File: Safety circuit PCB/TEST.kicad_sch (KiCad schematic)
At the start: 35 parts, among them J1 Conn_01x02_Socket, J2 Conn_01x02_Socket, J3 Conn_01x02_Socket, J4 Conn_01x02_Socket, J5 Conn_01x02_Socket, J6 Conn_01x01_Socket, J7 Conn_01x01_Socket, Q10 NMOS, Q11 NMOS, Q12 NMOS, Q6 NMOS, Q7 NMOS, Q8 NMOS, Q9 NMOS

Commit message: Safety Circuit PCB First Prototype
First prototype board and schematic for safety circuit. Falstad simulation for safety circuit demonstrating how it works is https://tinyurl.com/275r7dj9
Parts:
- removed J1, J2, J3, J4, J5: Conn_01x02_Socket, symbol Connector:Conn_01x02_Socket
- removed J6, J7: Conn_01x01_Socket, symbol Connector:Conn_01x01_Socket
- removed Q10, Q11, Q12, Q6, Q7, Q8, Q9: NMOS, symbol Simulation_SPICE:NMOS
- added J1, J2: 430450801, SC:CONN_SD-43045-001_08_MOL, symbol SC:430450801
- added Q1, Q2, Q3, Q4, Q5, Q6, Q7: 2N7002K, Package_TO_SOT_SMD:SOT-23, symbol Transistor_FET:2N7002K
- D10, D11, D12, D6, D7, D8, D9: footprint (none) -> SC:HL-PSC-1608U52GC-G4; JCL Datasheet (none) -> https://jlcpcb.com/api/file/downloadByFileSystemAccessId/85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; JCL Link (none) -> https://jlcpcb.com/partdetail/23857065-PSC_1608U50GCG4/C223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; JCL# (none) -> C22371297; MFR Part # (none) -> PSC-1608U50GC-G4; Manufacturer (none) -> HONGLITRONIC (Hongli Zhihui (HONGLITRONIC))
- R12, R13, R14, R15, R16, R17, R18, R19, R20, R21, R22, R23, R24, R25: value R_US -> 1k; footprint (none) -> SC:CRCW0805; Digikey (none) -> https://www.digikey.com/en/products/detail/vishay-dale/CRCW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; JCL Datasheet (none) -> https://jlcpcb.com/api/file/downloadByFileSystemAccessId/85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; JCL Link (none) -> https://jlcpcb.com/partdetail/VishayIntertech-CRCW08051K00F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; JCL# (none) -> C844939; MFR Part # (none) -> CRCW08051K00FKEA; Manufacturer (none) -> Vishay
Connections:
- net +12V: now also J2.8
- net BOTS: now also J2.2, J2.3, Q6.1 (G); no longer R12.1
- net COCKPIT_BUTTON: now also J1.8, J2.1, Q5.1 (G)
- net GND: now also J2.5, J2.6, J2.7, Q1.2 (S), Q2.2 (S), Q3.2 (S), Q4.2 (S), Q5.2 (S), Q6.2 (S), Q7.2 (S)
- net INERTIA_SWITCH: now also J1.6, J1.7, Q4.1 (G)
- net INPUT: now also J1.1, Q1.1 (G)
- net LEFT_BUTTON: now also J1.2, J1.3, Q2.1 (G)
- net RIGHT_BUTTON: now also J1.4, J1.5, Q3.1 (G)
- net at R19.2: now also Q6.3 (D)
- net at R25.2: now also Q1.3 (D)
- net at R20.2: now also Q5.3 (D)
- net at R21.2: now also Q4.3 (D)
- net at R22.2: now also Q3.3 (D)
- net at R18.2: now also Q7.3 (D)
- net at R23.2: now also Q2.3 (D)
- new net OUTPUT: J2.4, Q7.1 (G), R12.1

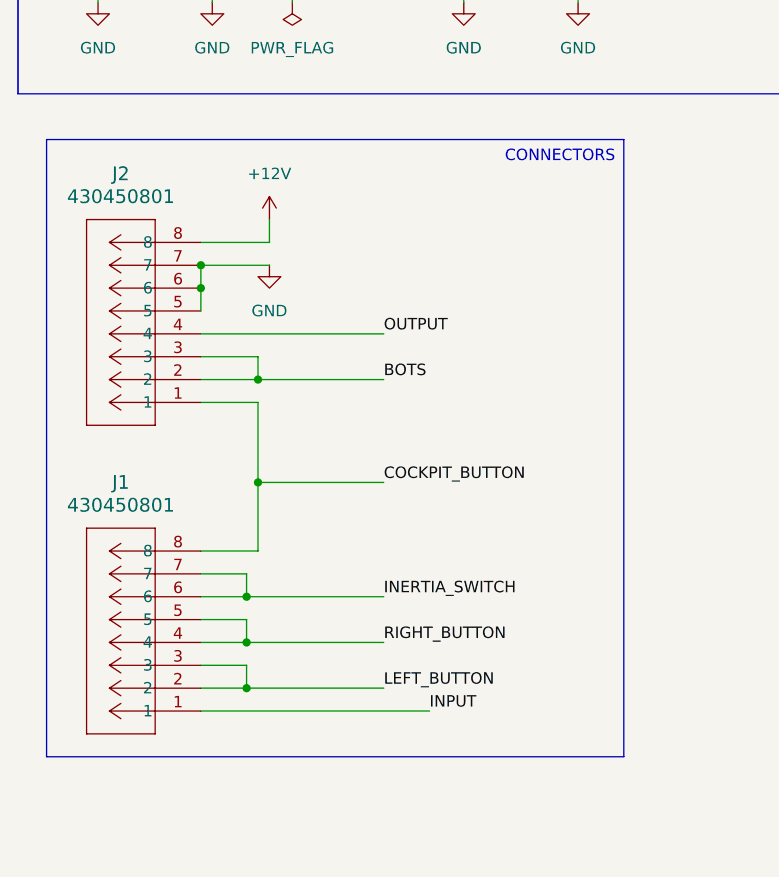
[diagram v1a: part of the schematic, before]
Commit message: Flip connectors, make more sane pin assignments for connections, get nicer tracks, and make dimensions reasonable
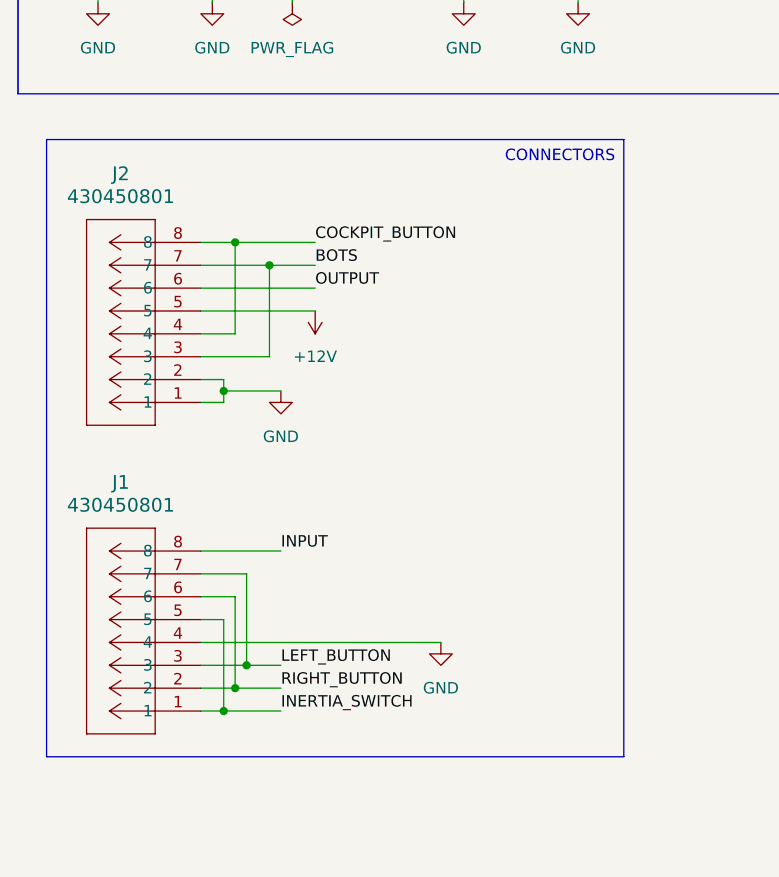
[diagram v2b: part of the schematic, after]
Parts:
- J1, J2: footprint SC:CONN_SD-43045-001_08_MOL -> CONN_SD-43045-001_08_MOL
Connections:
- net +12V: now also J2.5; no longer J2.8
- net BOTS: now also J2.7; no longer J2.2
- net COCKPIT_BUTTON: now also J2.4, J2.8; no longer J1.8, J2.1
- net GND: now also J1.4, J2.1, J2.2; no longer J2.5, J2.6, J2.7
- net INERTIA_SWITCH: now also J1.1, J1.5; no longer J1.6, J1.7
- net INPUT: now also J1.8; no longer J1.1
- net LEFT_BUTTON: now also J1.7; no longer J1.2
- net OUTPUT: now also J2.6; no longer J2.4
- net RIGHT_BUTTON: now also J1.2, J1.6; no longer J1.4, J1.5

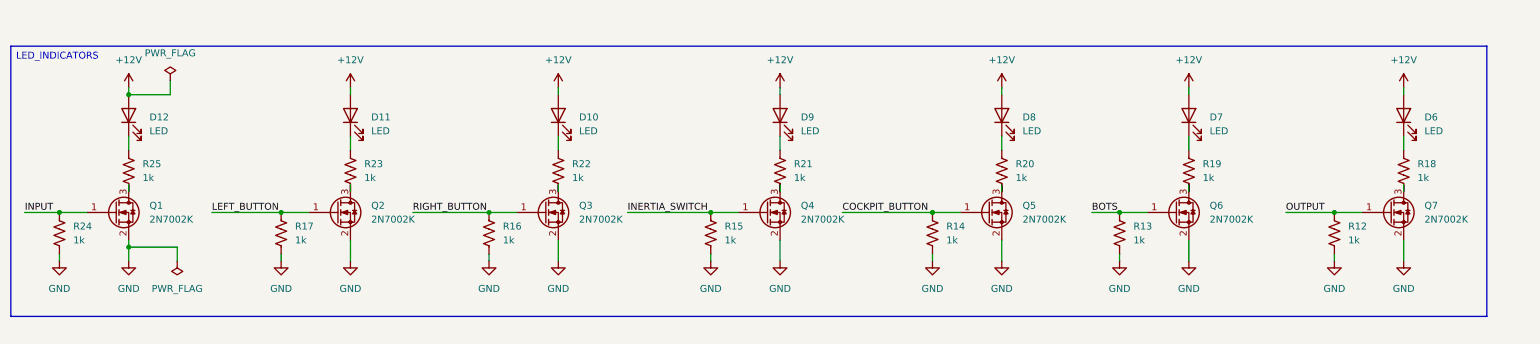
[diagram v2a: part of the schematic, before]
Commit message: Add mounting holes, round corners, add silkscreen logo and Charlie Brown
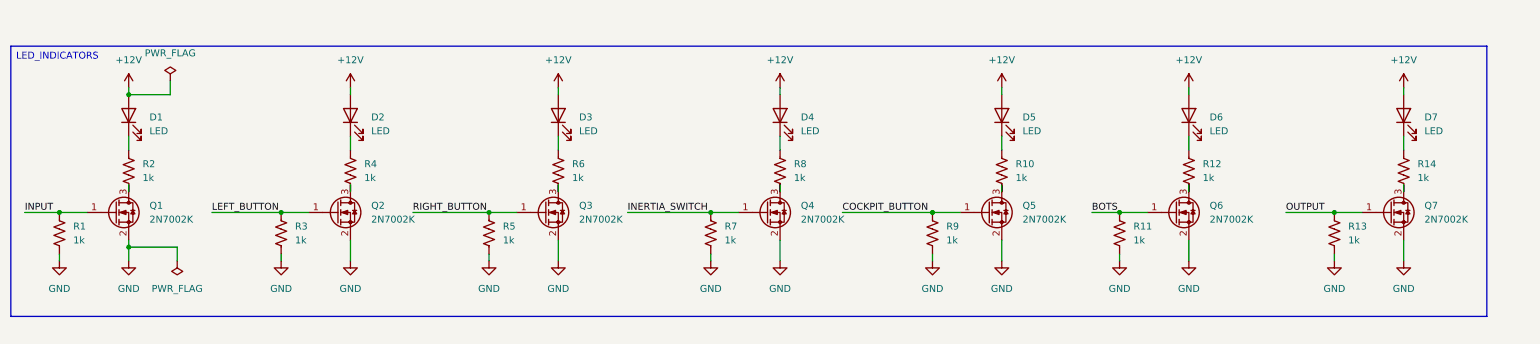
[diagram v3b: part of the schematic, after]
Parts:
- renumbered D12 to D1, D11 to D2, D10 to D3, D9 to D4, D8 to D5, D7 to D6, D6 to D7, R24 to R1, R20 to R10, R13 to R11, R19 to R12, R12 to R13, R18 to R14, R25 to R2, R17 to R3, R23 to R4, R16 to R5, R22 to R6, R15 to R7, R21 to R8, R14 to R9
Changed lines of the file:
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@@
 		(dnp no)
 		(fields_autoplaced yes)
-		(property "Reference" "R12"
+		(property "Reference" "R13"
 			(at 257.81 45.7199 0)
 			(effects
@@
 			)
 		)
-		(property "Datasheet" "~"
+		(property "Datasheet" "https://jlcpcb.com/api/file/downloadByFileSystemAccessId/8588950168741404672"
 			(at 255.27 46.99 0)
 			(effects
@@
 			(project "TEST"
 				(path "/49768109-2e19-4295-adfa-599621ab46ec"
-					(reference "R12")
+					(reference "R13")
 					(unit 1)
 				)
@@
 		(dnp no)
 		(fields_autoplaced yes)
-		(property "Reference" "D12"
+		(property "Reference" "D1"
 			(at 38.1 25.7174 90)
 			(effects
@@
 			)
 		)
-		(property "Datasheet" "~"
+		(property "Datasheet" "https://jlcpcb.com/api/file/downloadByFileSystemAccessId/8590916697501356032"
 			(at 34.29 25.4 0)
 			(effects
@@
 			(project "TEST"
 				(path "/49768109-2e19-4295-adfa-599621ab46ec"
-					(reference "D12")
+					(reference "D1")
 					(unit 1)
 				)
@@
 		(dnp no)
 		(fields_autoplaced yes)
-		(property "Reference" "D8"
+		(property "Reference" "D5"
 			(at 198.12 25.7174 90)
 			(effects
@@
 			)
 		)
-		(property "Datasheet" "~"
+		(property "Datasheet" "https://jlcpcb.com/api/file/downloadByFileSystemAccessId/8590916697501356032"
 			(at 194.31 25.4 0)
 			(effects
@@
 			(project "TEST"
 				(path "/49768109-2e19-4295-adfa-599621ab46ec"
-					(reference "D8")
+					(reference "D5")
 					(unit 1)
 				)
@@
 		(dnp no)
 		(fields_autoplaced yes)
-		(property "Reference" "R15"
+		(property "Reference" "R7"
 			(at 143.51 45.7199 0)
 			(effects
@@
 			)
 		)
-		(property "Datasheet" "~"
+		(property "Datasheet" "https://jlcpcb.com/api/file/downloadByFileSystemAccessId/8588950168741404672"
 			(at 140.97 46.99 0)
 			(effects
@@
 			(project "TEST"
 				(path "/49768109-2e19-4295-adfa-599621ab46ec"
-					(reference "R15")
+					(reference "R7")
 					(unit 1)
 				)
@@
 		(dnp no)
 		(fields_autoplaced yes)
-		(property "Reference" "R13"
+		(property "Reference" "R11"
 			(at 218.44 45.7199 0)
 			(effects
@@
 			)
 		)
-		(property "Datasheet" "~"
+		(property "Datasheet" "https://jlcpcb.com/api/file/downloadByFileSystemAccessId/8588950168741404672"
 			(at 215.9 46.99 0)
 			(effects
@@
 			(project "TEST"
 				(path "/49768109-2e19-4295-adfa-599621ab46ec"
-					(reference "R13")
+					(reference "R11")
 					(unit 1)
 				)
@@
 		(dnp no)
 		(fields_autoplaced yes)
-		(property "Reference" "D11"
+		(property "Reference" "D2"
 			(at 78.74 25.7174 90)
 			(effects
@@
 			)
 		)
-		(property "Datasheet" "~"
+		(property "Datasheet" "https://jlcpcb.com/api/file/downloadByFileSystemAccessId/8590916697501356032"
 			(at 74.93 25.4 0)
 			(effects
@@
 			(project "TEST"
 				(path "/49768109-2e19-4295-adfa-599621ab46ec"
-					(reference "D11")
+					(reference "D2")
 					(unit 1)
 				)
@@
 		(dnp no)
 		(fields_autoplaced yes)
-		(property "Reference" "R17"
+		(property "Reference" "R3"
 			(at 64.77 45.7199 0)
 			(effects
@@
 			)
 		)
-		(property "Datasheet" "~"
+		(property "Datasheet" "https://jlcpcb.com/api/file/downloadByFileSystemAccessId/8588950168741404672"
 			(at 62.23 46.99 0)
 			(effects
@@
 			(project "TEST"
 				(path "/49768109-2e19-4295-adfa-599621ab46ec"
-					(reference "R17")
+					(reference "R3")
 					(unit 1)
 				)
@@
 		(dnp no)
 		(fields_autoplaced yes)
-		(property "Reference" "R20"
+		(property "Reference" "R10"
 			(at 196.85 34.2899 0)
 			(effects
@@
 			)
 		)
-		(property "Datasheet" "~"
+		(property "Datasheet" "https://jlcpcb.com/api/file/downloadByFileSystemAccessId/8588950168741404672"
 			(at 194.31 35.56 0)
 			(effects
@@
 			(project "TEST"
 				(path "/49768109-2e19-4295-adfa-599621ab46ec"
-					(reference "R20")
+					(reference "R10")
 					(unit 1)
 				)
@@
 		(dnp no)
 		(fields_autoplaced yes)
-		(property "Reference" "R19"
+		(property "Reference" "R12"
 			(at 231.14 34.2899 0)
 			(effects
@@
 			)
 		)
-		(property "Datasheet" "~"
+		(property "Datasheet" "https://jlcpcb.com/api/file/downloadByFileSystemAccessId/8588950168741404672"
 			(at 228.6 35.56 0)
 			(effects
@@
 			(project "TEST"
 				(path "/49768109-2e19-4295-adfa-599621ab46ec"
-					(reference "R19")
+					(reference "R12")
 					(unit 1)
 				)
@@
 		(dnp no)
 		(fields_autoplaced yes)
-		(property "Reference" "D6"
+		(property "Reference" "D7"
 			(at 271.78 25.7174 90)
 			(effects
@@
 			)
 		)
-		(property "Datasheet" "~"
+		(property "Datasheet" "https://jlcpcb.com/api/file/downloadByFileSystemAccessId/8590916697501356032"
 			(at 267.97 25.4 0)
 			(effects
@@
 			(project "TEST"
 				(path "/49768109-2e19-4295-adfa-599621ab46ec"
-					(reference "D6")
+					(reference "D7")
 					(unit 1)
 				)
@@
 		(dnp no)
 		(fields_autoplaced yes)
-		(property "Reference" "R24"
+		(property "Reference" "R1"
 			(at 24.13 45.7199 0)
 			(effects
@@
 			)
 		)
-		(property "Datasheet" "~"
+		(property "Datasheet" "https://jlcpcb.com/api/file/downloadByFileSystemAccessId/8588950168741404672"
 			(at 21.59 46.99 0)
 			(effects
@@
 			(project "TEST"
 				(path "/49768109-2e19-4295-adfa-599621ab46ec"
-					(reference "R24")
+					(reference "R1")
 					(unit 1)
 				)
@@
 		(dnp no)
 		(fields_autoplaced yes)
-		(property "Reference" "D7"
+		(property "Reference" "D6"
 			(at 232.41 25.7174 90)
 			(effects
@@
 			)
 		)
-		(property "Datasheet" "~"
+		(property "Datasheet" "https://jlcpcb.com/api/file/downloadByFileSystemAccessId/8590916697501356032"
 			(at 228.6 25.4 0)
 			(effects
@@
 			(project "TEST"
 				(path "/49768109-2e19-4295-adfa-599621ab46ec"
-					(reference "D7")
+					(reference "D6")
 					(unit 1)
 				)
@@
 		(dnp no)
 		(fields_autoplaced yes)
-		(property "Reference" "R22"
+		(property "Reference" "R6"
 			(at 115.57 34.2899 0)
 			(effects
@@
 			)
 		)
-		(property "Datasheet" "~"
+		(property "Datasheet" "https://jlcpcb.com/api/file/downloadByFileSystemAccessId/8588950168741404672"
 			(at 113.03 35.56 0)
 			(effects
@@
 			(project "TEST"
 				(path "/49768109-2e19-4295-adfa-599621ab46ec"
-					(reference "R22")
+					(reference "R6")
 					(unit 1)
 				)
@@
 		(dnp no)
 		(fields_autoplaced yes)
-		(property "Reference" "R18"
+		(property "Reference" "R14"
 			(at 270.51 34.2899 0)
 			(effects
@@
 			)
 		)
-		(property "Datasheet" "~"
+		(property "Datasheet" "https://jlcpcb.com/api/file/downloadByFileSystemAccessId/8588950168741404672"
 			(at 267.97 35.56 0)
 			(effects
@@
 			(project "TEST"
 				(path "/49768109-2e19-4295-adfa-599621ab46ec"
-					(reference "R18")
+					(reference "R14")
 					(unit 1)
 				)
@@
 		(dnp no)
 		(fields_autoplaced yes)
-		(property "Reference" "R23"
+		(property "Reference" "R4"
 			(at 77.47 34.2899 0)
 			(effects
@@
 			)
 		)
-		(property "Datasheet" "~"
+		(property "Datasheet" "https://jlcpcb.com/api/file/downloadByFileSystemAccessId/8588950168741404672"
 			(at 74.93 35.56 0)
 			(effects
@@
 			(project "TEST"
 				(path "/49768109-2e19-4295-adfa-599621ab46ec"
-					(reference "R23")
+					(reference "R4")
 					(unit 1)
 				)
@@
 		(dnp no)
 		(fields_autoplaced yes)
-		(property "Reference" "D10"
+		(property "Reference" "D3"
 			(at 116.84 25.7174 90)
 			(effects
@@
 			)
 		)
-		(property "Datasheet" "~"
+		(property "Datasheet" "https://jlcpcb.com/api/file/downloadByFileSystemAccessId/8590916697501356032"
 			(at 113.03 25.4 0)
 			(effects
@@
 			(project "TEST"
 				(path "/49768109-2e19-4295-adfa-599621ab46ec"
-					(reference "D10")
+					(reference "D3")
 					(unit 1)
 				)
@@
 		(dnp no)
 		(fields_autoplaced yes)
-		(property "Reference" "R25"
+		(property "Reference" "R2"
 			(at 36.83 34.2899 0)
 			(effects
@@
 			)
 		)
-		(property "Datasheet" "~"
+		(property "Datasheet" "https://jlcpcb.com/api/file/downloadByFileSystemAccessId/8588950168741404672"
 			(at 34.29 35.56 0)
 			(effects
@@
 			(project "TEST"
 				(path "/49768109-2e19-4295-adfa-599621ab46ec"
-					(reference "R25")
+					(reference "R2")
 					(unit 1)
 				)
@@
 		(dnp no)
 		(fields_autoplaced yes)
-		(property "Reference" "R21"
+		(property "Reference" "R8"
 			(at 156.21 34.2899 0)
 			(effects
@@
 			)
 		)
-		(property "Datasheet" "~"
+		(property "Datasheet" "https://jlcpcb.com/api/file/downloadByFileSystemAccessId/8588950168741404672"
 			(at 153.67 35.56 0)
 			(effects
@@
 			(project "TEST"
 				(path "/49768109-2e19-4295-adfa-599621ab46ec"
-					(reference "R21")
+					(reference "R8")
 					(unit 1)
 				)
@@
 		(dnp no)
 		(fields_autoplaced yes)
-		(property "Reference" "R14"
+		(property "Reference" "R9"
 			(at 184.15 45.7199 0)
 			(effects
@@
 			)
 		)
-		(property "Datasheet" "~"
+		(property "Datasheet" "https://jlcpcb.com/api/file/downloadByFileSystemAccessId/8588950168741404672"
 			(at 181.61 46.99 0)
 			(effects
@@
 			(project "TEST"
 				(path "/49768109-2e19-4295-adfa-599621ab46ec"
-					(reference "R14")
+					(reference "R9")
 					(unit 1)
 				)
@@
 		(on_board yes)
 		(dnp no)
-		(property "Reference" "R16"
+		(property "Reference" "R5"
 			(at 102.87 45.7199 0)
 			(effects
@@
 			)
 		)
-		(property "Datasheet" "~"
+		(property "Datasheet" "https://jlcpcb.com/api/file/downloadByFileSystemAccessId/8588950168741404672"
 			(at 100.33 46.99 0)
 			(effects
@@
 			(project "TEST"
 				(path "/49768109-2e19-4295-adfa-599621ab46ec"
-					(reference "R16")
+					(reference "R5")
 					(unit 1)
 				)
@@
 		(dnp no)
 		(fields_autoplaced yes)
-		(property "Reference" "D9"
+		(property "Reference" "D4"
 			(at 157.48 25.7174 90)
 			(effects
@@
 			)
 		)
-		(property "Datasheet" "~"
+		(property "Datasheet" "https://jlcpcb.com/api/file/downloadByFileSystemAccessId/8590916697501356032"
 			(at 153.67 25.4 0)
 			(effects
@@
 			(project "TEST"
 				(path "/49768109-2e19-4295-adfa-599621ab46ec"
-					(reference "D9")
+					(reference "D4")
 					(unit 1)
 				)
